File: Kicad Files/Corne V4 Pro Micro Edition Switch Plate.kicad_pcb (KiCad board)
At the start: 2 copper layers, 135.1 x 94.4 mm, 0 parts

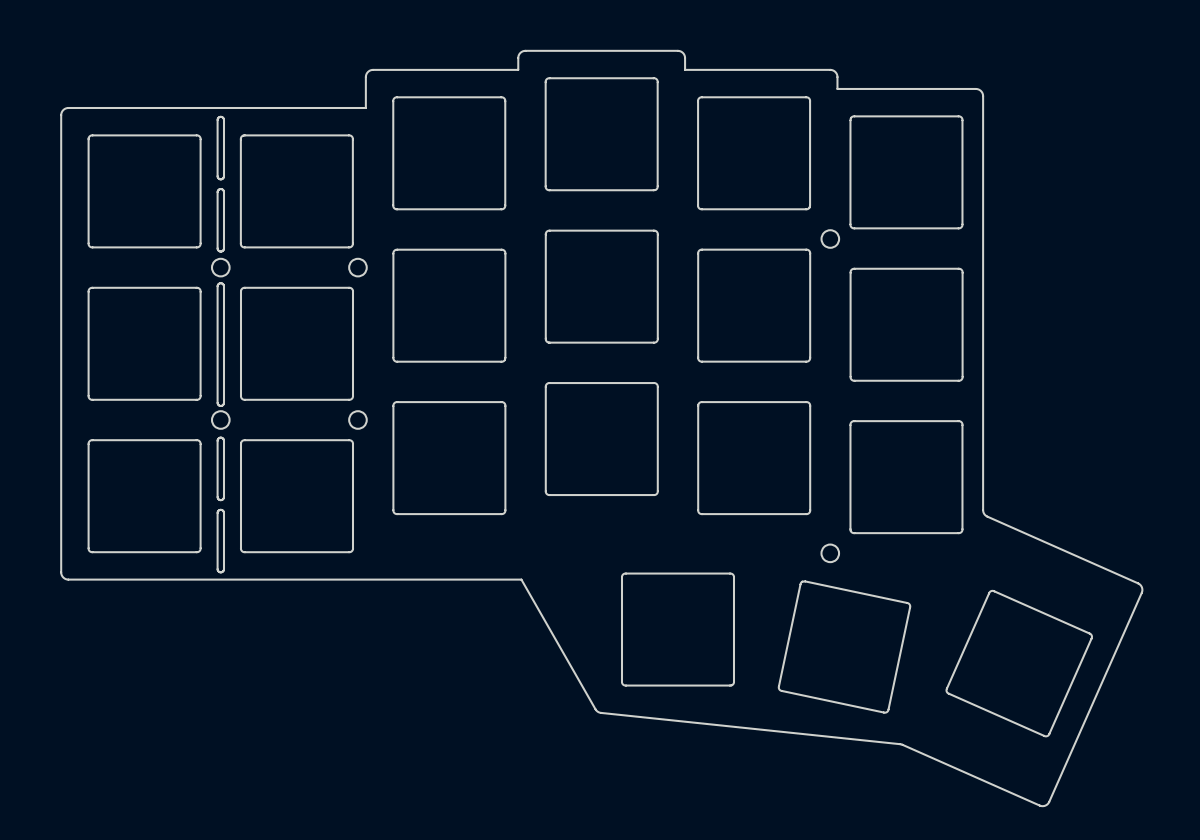
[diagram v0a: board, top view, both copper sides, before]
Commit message: add logo and copper zone (copied from main PCB)
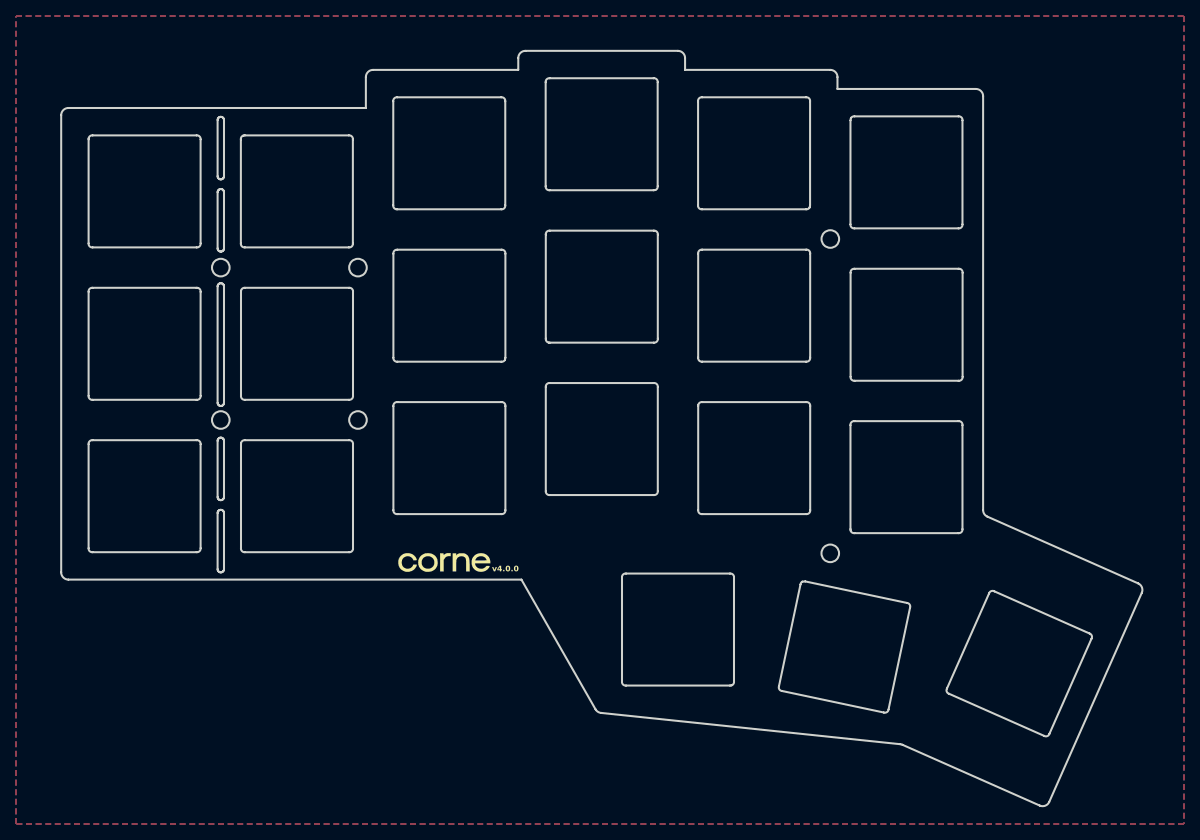
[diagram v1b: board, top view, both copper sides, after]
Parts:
- added G***: LOGO, kbd:corne-logo-horizontal, F.Cu at (127.1, 110.4)
- added G***: LOGO, kbd:corne-logo-horizontal, B.Cu at (126.9, 110.4)
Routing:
- added copper zone on B.Cu, net (none)
- added copper zone on F.Cu, net (none)
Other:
- board text added: "v4.0.0"
